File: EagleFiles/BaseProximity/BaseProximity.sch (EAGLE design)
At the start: 30 parts

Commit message: v1 of proximity board completed
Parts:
- removed JP1: (no value), pinhead:PINHD-1X2
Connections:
- removed net VIN: JP1.1
- net +5V: now also LED1.A
- net GND: no longer JP1.2
- net VCC: no longer LED1.A
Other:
- note removed: "(for low power aplications)"
- note removed: "Power isolation jumper"
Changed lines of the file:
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@@
 <part name="JP3" library="pinhead" deviceset="PINHD-1X3" device=""/>
 <part name="JP4" library="pinhead" deviceset="PINHD-1X3" device=""/>
-<part name="JP1" library="pinhead" deviceset="PINHD-1X2" device=""/>
 <part name="JP7" library="pinhead" deviceset="PINHD-1X4" device=""/>
 <part name="R1" library="SparkFun" deviceset="RESISTOR" device="0603-RES" value="330"/>
@@
 <text x="165.862" y="9.144" size="1.778" layer="94">Kevin D. Wolf - Software Logistics</text>
 <text x="240.284" y="7.366" size="1.778" layer="94">14</text>
-<text x="58.42" y="177.8" size="1.778" layer="97">Power isolation jumper</text>
-<text x="56.642" y="175.006" size="1.778" layer="97">(for low power aplications)</text>
-<wire x1="66.04" y1="172.72" x2="67.818" y2="167.64" width="0.2032" layer="97"/>
-<wire x1="67.818" y1="167.64" x2="68.072" y2="169.164" width="0.2032" layer="97"/>
 <wire x1="67.818" y1="167.64" x2="66.548" y2="168.402" width="0.2032" layer="97"/>
 </plain>
@@
 <instance part="JP3" gate="A" x="142.24" y="170.18"/>
 <instance part="JP4" gate="A" x="142.24" y="154.94"/>
-<instance part="JP1" gate="G$1" x="190.5" y="170.18"/>
 <instance part="JP7" gate="A" x="226.06" y="165.1"/>
 <instance part="R1" gate="G$1" x="180.34" y="88.9" rot="R270"/>
@@
 </segment>
 <segment>
-<pinref part="JP1" gate="G$1" pin="2"/>
-<wire x1="187.96" y1="170.18" x2="167.64" y2="170.18" width="0.1524" layer="91"/>
-<label x="172.72" y="170.18" size="1.778" layer="95"/>
-</segment>
-<segment>
 <pinref part="JP7" gate="A" pin="4"/>
 <wire x1="223.52" y1="162.56" x2="208.28" y2="162.56" width="0.1524" layer="91"/>
@@
 <pinref part="P+4" gate="G$1" pin="3.3V"/>
 <wire x1="86.36" y1="165.1" x2="86.36" y2="162.56" width="0.1524" layer="91"/>
-<wire x1="86.36" y1="162.56" x2="83.82" y2="162.56" width="0.1524" layer="91"/>
 <pinref part="C13" gate="G$1" pin="+"/>
-<wire x1="83.82" y1="162.56" x2="76.2" y2="162.56" width="0.1524" layer="91"/>
+<wire x1="86.36" y1="162.56" x2="76.2" y2="162.56" width="0.1524" layer="91"/>
 <wire x1="76.2" y1="160.02" x2="76.2" y2="162.56" width="0.1524" layer="91"/>
-<junction x="76.2" y="162.56"/>
-<wire x1="83.82" y1="160.02" x2="83.82" y2="162.56" width="0.1524" layer="91"/>
-<junction x="83.82" y="162.56"/>
-<pinref part="LED1" gate="G$1" pin="A"/>
-<wire x1="60.96" y1="162.56" x2="63.5" y2="162.56" width="0.1524" layer="91"/>
-<wire x1="60.96" y1="160.02" x2="60.96" y2="162.56" width="0.1524" layer="91"/>
-<junction x="60.96" y="162.56"/>
-<wire x1="60.96" y1="162.56" x2="76.2" y2="162.56" width="0.1524" layer="91"/>
 </segment>
 <segment>
@@
 <label x="208.28" y="170.18" size="1.778" layer="95"/>
 </segment>
+<segment>
+<pinref part="LED1" gate="G$1" pin="A"/>
+<wire x1="60.96" y1="160.02" x2="60.96" y2="162.56" width="0.1524" layer="91"/>
+</segment>
 </net>
 <net name="N$9" class="0">
@@
 </segment>
 </net>
-<net name="VIN" class="0">
-<segment>
-<pinref part="JP1" gate="G$1" pin="1"/>
-<wire x1="187.96" y1="172.72" x2="167.64" y2="172.72" width="0.1524" layer="91"/>
-<label x="172.72" y="172.72" size="1.778" layer="95"/>
-</segment>
-</net>

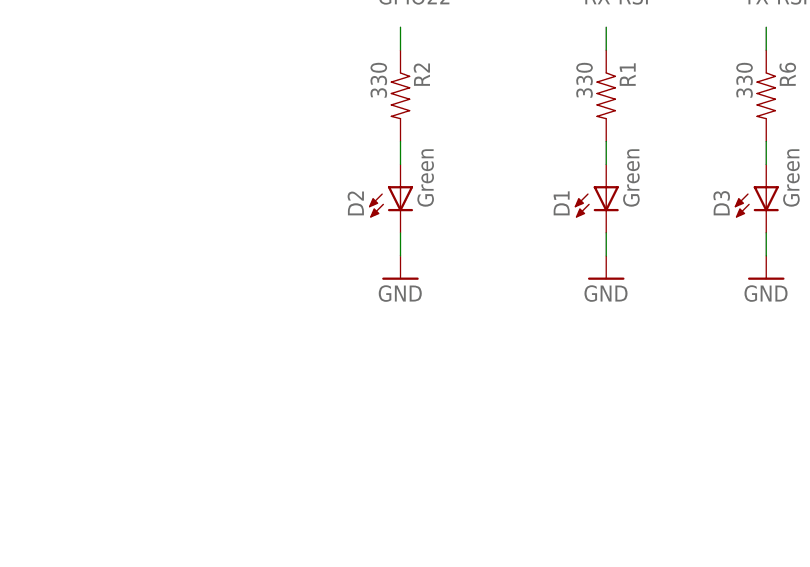
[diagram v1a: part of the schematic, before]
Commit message: add shopping list and getting started
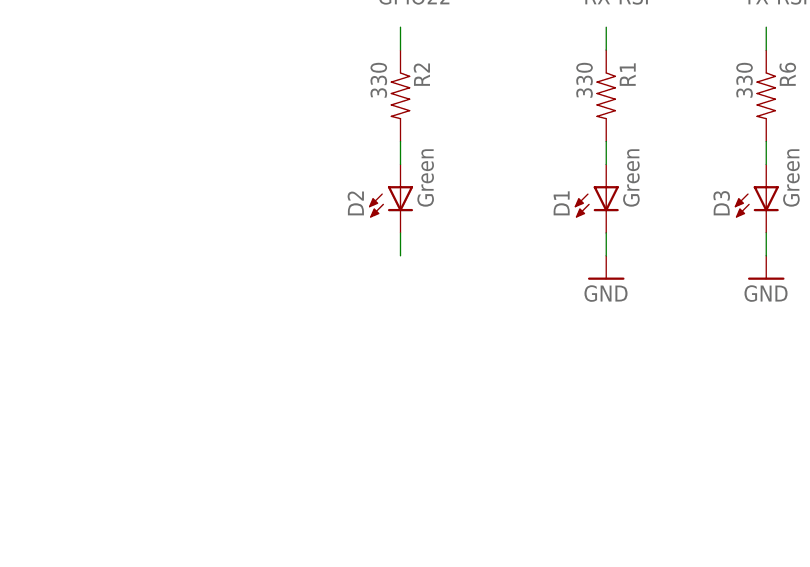
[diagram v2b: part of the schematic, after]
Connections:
- net GND: no longer D2.C
- net VCC: now also D2.C
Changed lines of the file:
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@@
 <part name="R2" library="SparkFun" deviceset="RESISTOR" device="0603-RES" value="330"/>
 <part name="D2" library="Testing" deviceset="LED" device="" value="Green"/>
-<part name="GND2" library="SparkFun" deviceset="GND" device=""/>
 </parts>
 <sheets>
@@
 <attribute name="VALUE" x="161.163" y="76.454" size="1.778" layer="96" rot="R90"/>
 </instance>
-<instance part="GND2" gate="1" x="157.48" y="68.58"/>
 </instances>
 <busses>
@@
 <pinref part="GND1" gate="1" pin="GND"/>
 </segment>
-<segment>
-<wire x1="157.48" y1="71.12" x2="157.48" y2="73.66" width="0.1524" layer="91"/>
-<pinref part="D2" gate="G$1" pin="C"/>
-<pinref part="GND2" gate="1" pin="GND"/>
-</segment>
 </net>
 <net name="N$7" class="0">
@@
 <label x="35.56" y="22.86" size="1.778" layer="95"/>
 </segment>
+<segment>
+<wire x1="157.48" y1="71.12" x2="157.48" y2="73.66" width="0.1524" layer="91"/>
+<pinref part="D2" gate="G$1" pin="C"/>
+</segment>
 </net>

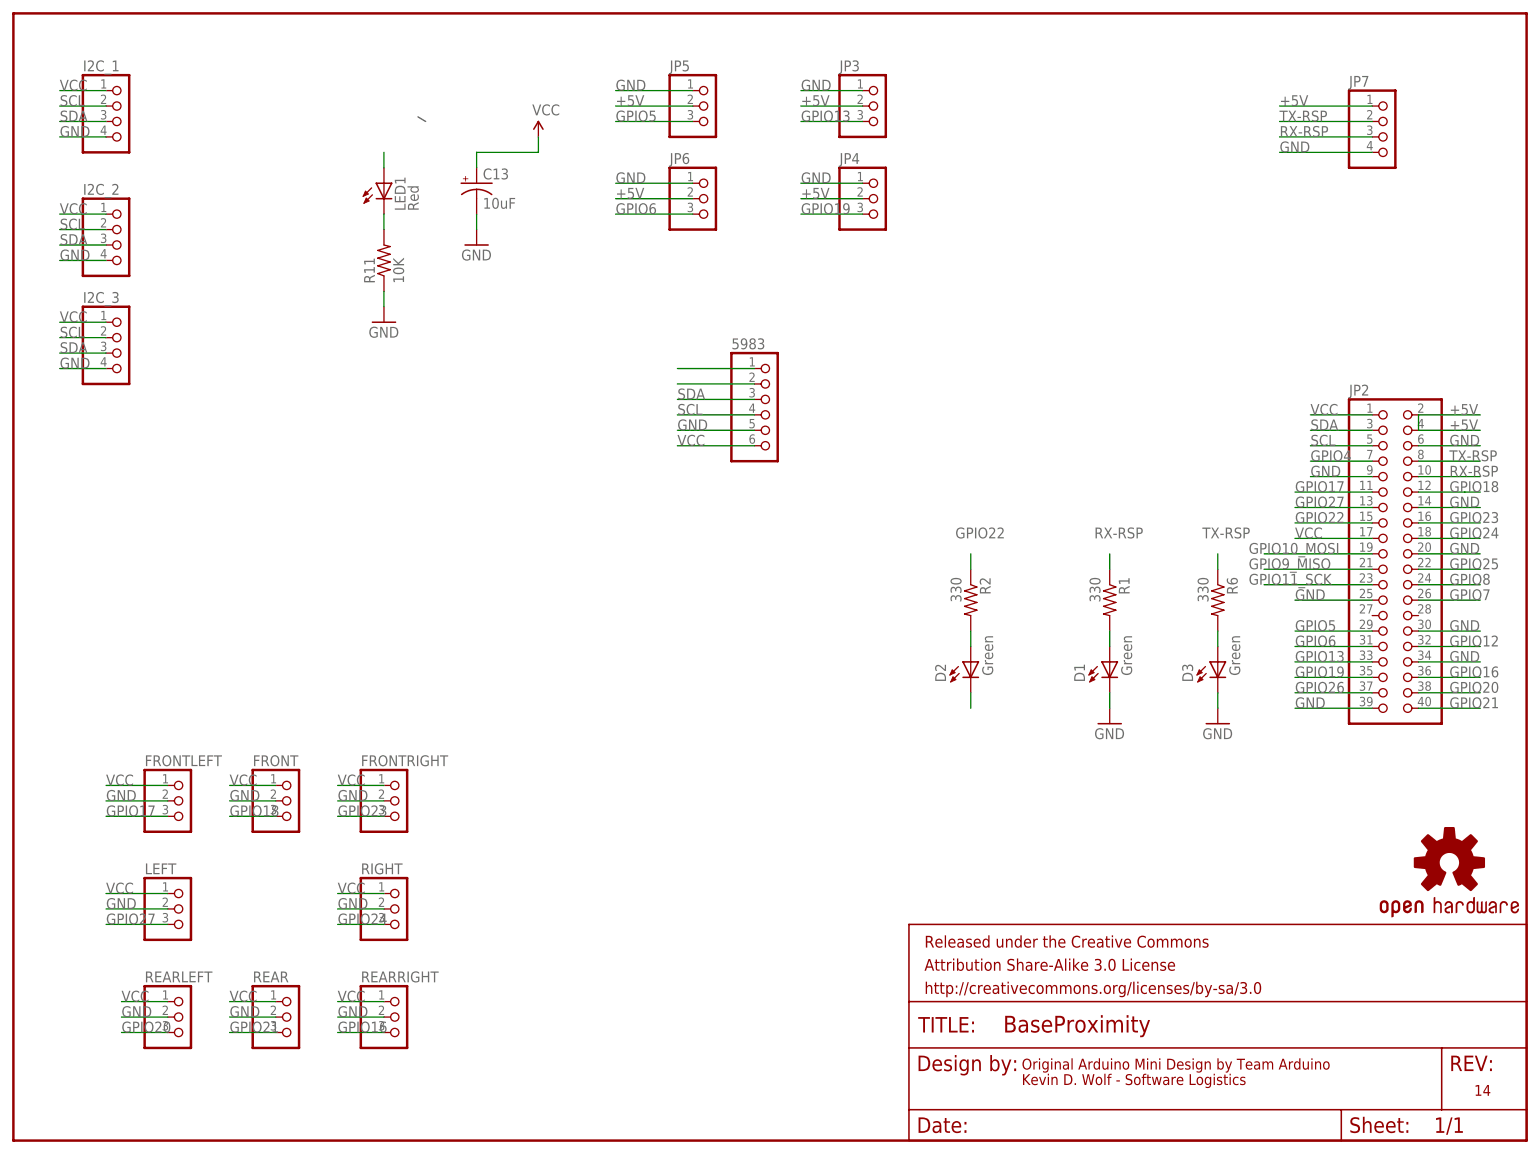
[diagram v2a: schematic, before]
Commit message: updated dox, and stubs for controlling with XBox Controller
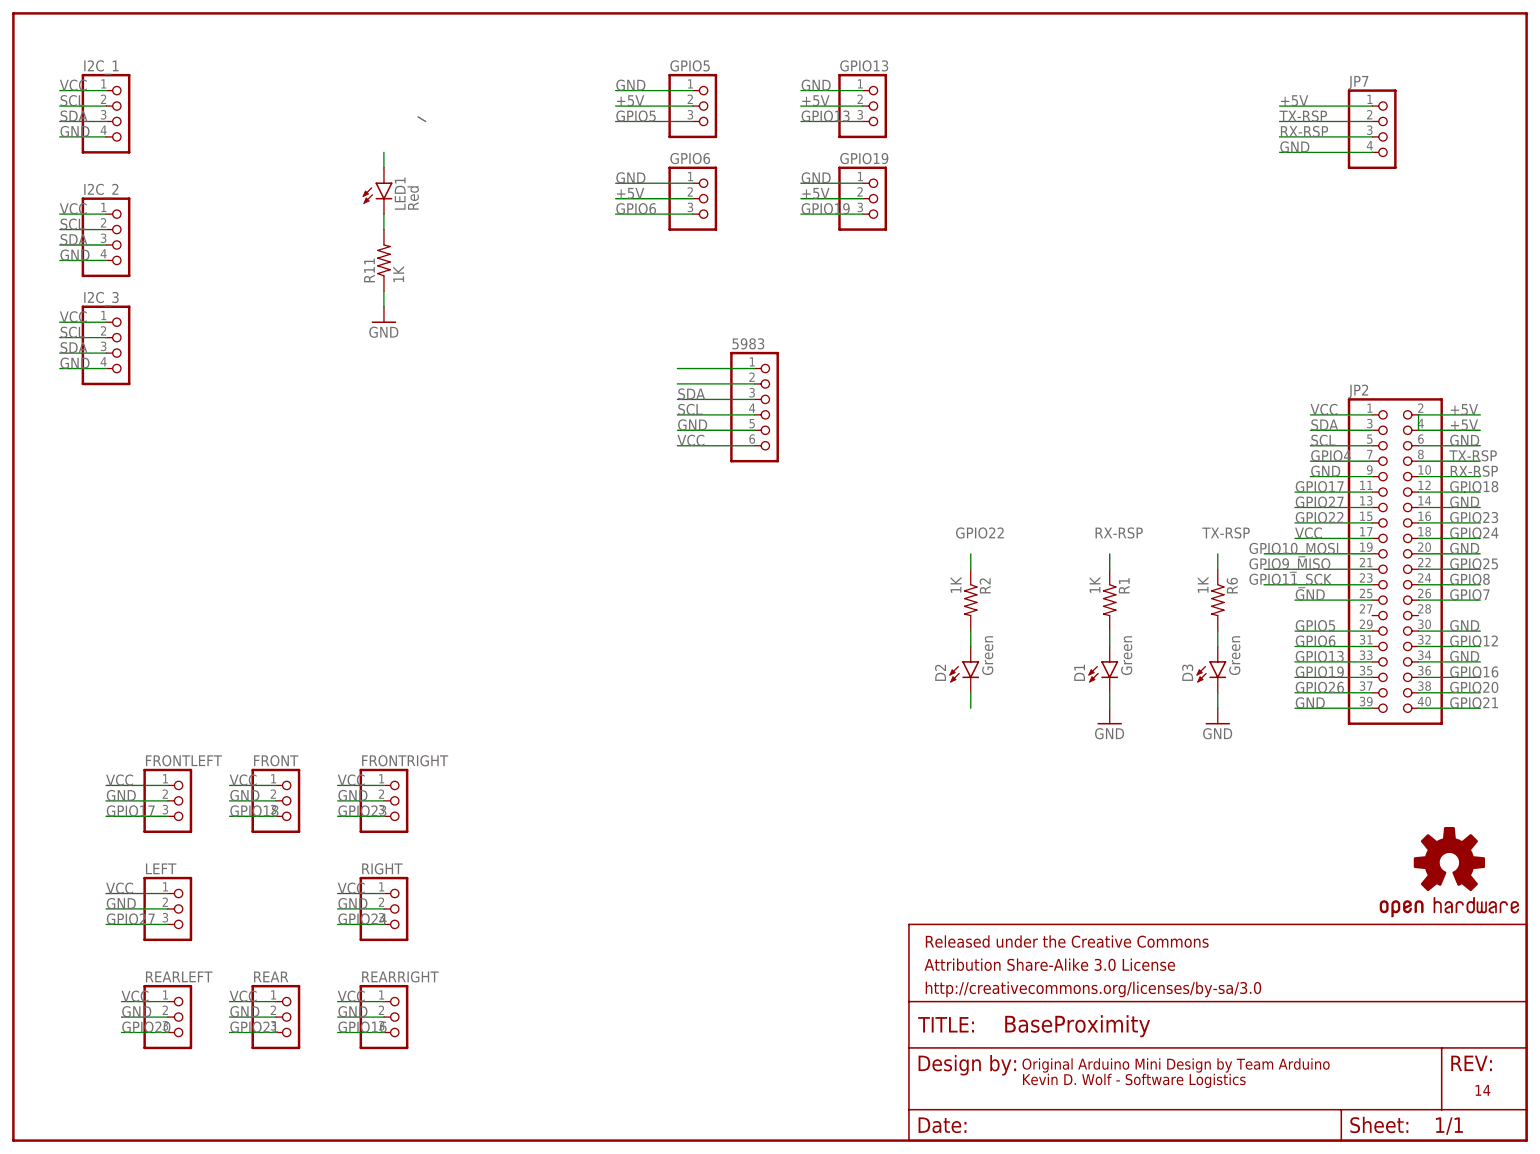
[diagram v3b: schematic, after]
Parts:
- removed C13: 10uF, SparkFun:CAP_POL1206
- D1, D2, D3, LED1: device Testing:LED -> SparkFun-LED:LED5MM
- R1, R2, R6: value 330 -> 1K; device SparkFun:RESISTOR0603-RES -> SparkFun-Resistors:1KOHM-1/4W-1%(PTH)
- R11: value 10K -> 1K; device SparkFun:RESISTOR0603-RES -> SparkFun-Resistors:1KOHM-1/4W-1%(PTH)
- renumbered JP3 to GPIO13, JP4 to GPIO19, JP5 to GPIO5, JP6 to GPIO6
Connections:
- net GND: no longer C13.-
- net VCC: no longer C13.+

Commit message: board design w/ switch IR
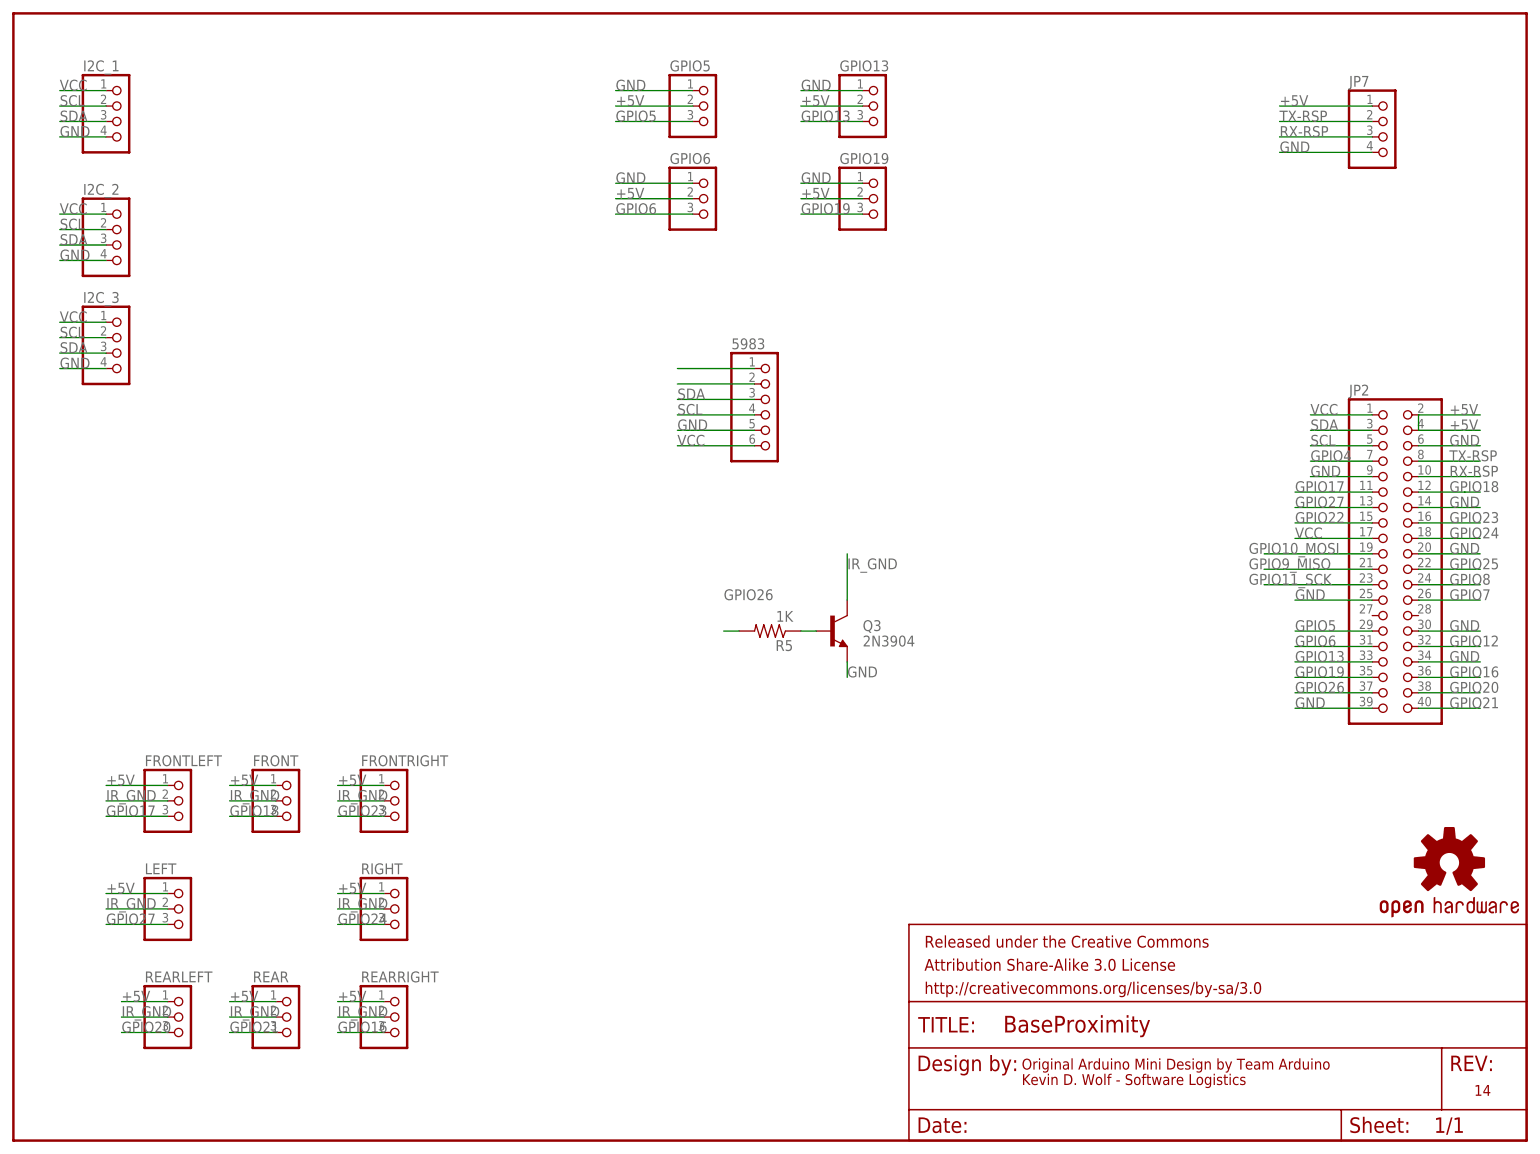
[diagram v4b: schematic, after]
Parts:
- removed D1, D2, D3: Green, SparkFun-LED:LED5MM
- removed LED1: Red, SparkFun-LED:LED5MM
- removed R1, R11, R2, R6: 1K, SparkFun-Resistors:1KOHM-1/4W-1%(PTH)
- added Q3: 2N3904, SparkFun-DiscreteSemi:TRANSISTOR_NPN2N3904-EZ
- added R5: 1K, SparkFun-Resistors:1KOHM-1/4W-1%(PTH)HORIZ-KIT
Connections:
- removed net N$1: D1.A, R1.2
- removed net N$2: D2.A, R2.2
- removed net N$4: LED1.C, R11.2
- removed net N$7: D3.A, R6.2
- new net IR_GND: FRONT.2, FRONTLEFT.2, FRONTRIGHT.2, LEFT.2, Q3.C, REAR.2, REARLEFT.2, REARRIGHT.2, RIGHT.2
- new net N$3: Q3.B, R5.1
- net +5V: now also FRONT.1, FRONTLEFT.1, FRONTRIGHT.1, LEFT.1, REAR.1, REARLEFT.1, REARRIGHT.1, RIGHT.1; no longer LED1.A
- net GND: now also Q3.E; no longer D1.C, D3.C, FRONT.2, FRONTLEFT.2, FRONTRIGHT.2, LEFT.2, R11.1, REAR.2, REARLEFT.2, REARRIGHT.2, RIGHT.2
- net GPIO22: no longer R2.1
- net GPIO26: now also R5.2
- net RX-RSP: no longer R1.1
- net TX-RSP: no longer R6.1
- net VCC: no longer D2.C, FRONT.1, FRONTLEFT.1, FRONTRIGHT.1, LEFT.1, REAR.1, REARLEFT.1, REARRIGHT.1, RIGHT.1
